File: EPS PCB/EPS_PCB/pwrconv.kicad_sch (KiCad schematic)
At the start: 27 parts, among them U1 TPS5430DDA, U2 TPS5430DDA, U3 TPS5430DDA

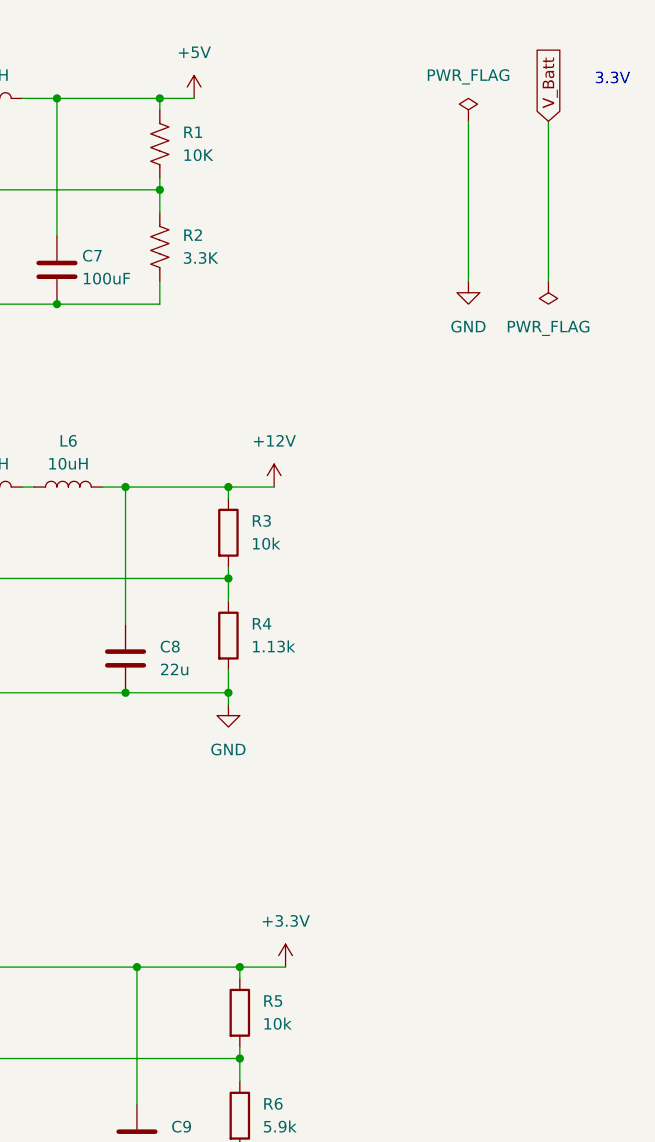
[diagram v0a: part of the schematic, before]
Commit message: PDR Update
Added Current Measurement, Hysteresis, EFuses
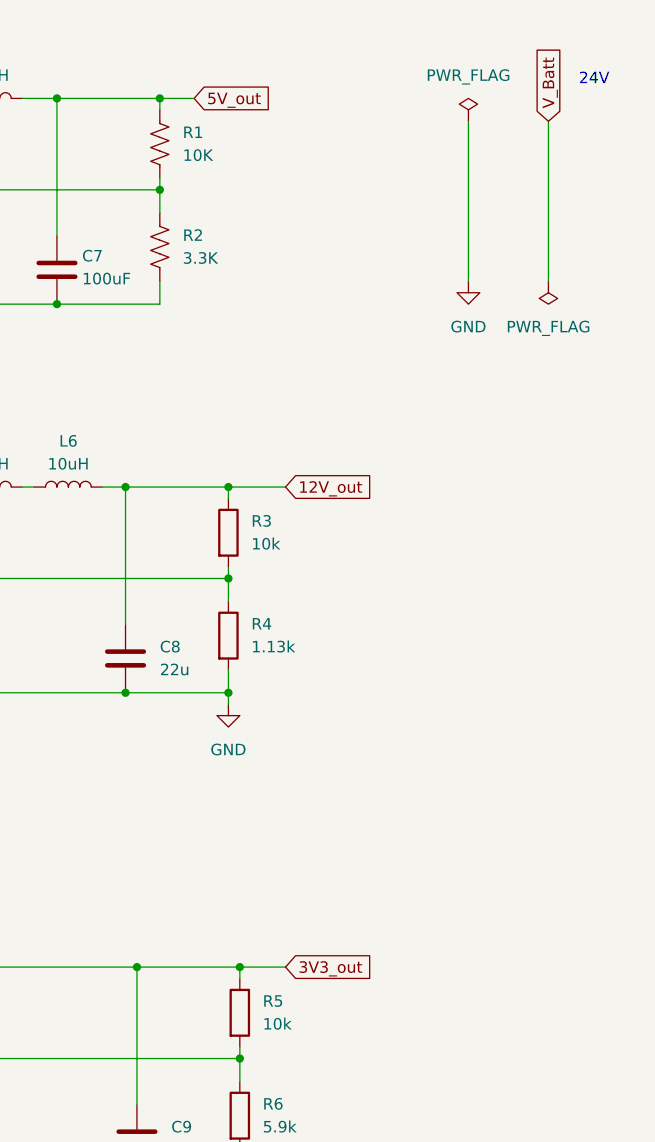
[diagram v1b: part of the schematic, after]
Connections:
- net +12V renamed 12V_out
- net +3.3V renamed 3V3_out
- net +5V renamed 5V_out
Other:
- note added: "24V"
- note removed: "3.3V"
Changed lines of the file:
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@@
 		(date "2024-11-14")
 		(company "UW Huskysat")
-		(comment 1 "Tracy, Maria, Phina, David")
-	)
-	(text "3.3V\n"
+		(comment 1 "Tracy, Maria, Phina, David, Chase")
+	)
+	(text "24V\n"
 		(exclude_from_sim no)
-		(at 188.722 22.098 0)
+		(at 186.69 22.098 0)
 		(effects
 			(font
@@
 	(wire
 		(pts
-			(xy 146.05 67.31) (xy 151.13 67.31)
+			(xy 146.05 67.31) (xy 152.4 67.31)
 		)
 		(stroke
@@
 		)
 	)
+	(global_label "3V3_out"
+		(shape input)
+		(at 152.4 120.65 0)
+		(fields_autoplaced yes)
+		(effects
+			(font
+				(size 1.27 1.27)
+			)
+			(justify left)
+		)
+		(property "Intersheetrefs" "${INTERSHEET_REFS}"
+			(at 162.8841 120.65 0)
+			(effects
+				(font
+					(size 1.27 1.27)
+				)
+				(justify left)
+				(hide yes)
+			)
+		)
+	)
 	(global_label "V_Batt"
 		(shape input)
@@
 				)
 				(justify right)
+				(hide yes)
+			)
+		)
+	)
+	(global_label "5V_out"
+		(shape input)
+		(at 142.24 24.13 0)
+		(fields_autoplaced yes)
+		(effects
+			(font
+				(size 1.27 1.27)
+			)
+			(justify left)
+		)
+		(property "Intersheetrefs" "${INTERSHEET_REFS}"
+			(at 151.5146 24.13 0)
+			(effects
+				(font
+					(size 1.27 1.27)
+				)
+				(justify left)
+				(hide yes)
+			)
+		)
+	)
+	(global_label "12V_out"
+		(shape input)
+		(at 152.4 67.31 0)
+		(fields_autoplaced yes)
+		(effects
+			(font
+				(size 1.27 1.27)
+			)
+			(justify left)
+		)
+		(property "Intersheetrefs" "${INTERSHEET_REFS}"
+			(at 162.8841 67.31 0)
+			(effects
+				(font
+					(size 1.27 1.27)
+				)
+				(justify left)
 				(hide yes)
 			)
@@
 	)
 	(symbol
-		(lib_id "power:+12V")
-		(at 151.13 67.31 0)
-		(unit 1)
-		(exclude_from_sim no)
-		(in_bom yes)
-		(on_board yes)
-		(dnp no)
-		(fields_autoplaced yes)
-		(property "Reference" "#PWR014"
-			(at 151.13 71.12 0)
-			(effects
-				(font
-					(size 1.27 1.27)
-				)
-				(hide yes)
-			)
-		)
-		(property "Value" "+12V"
-			(at 151.13 62.23 0)
-			(effects
-				(font
-					(size 1.27 1.27)
-				)
-			)
-		)
-		(property "Footprint" ""
-			(at 151.13 67.31 0)
-			(effects
-				(font
-					(size 1.27 1.27)
-				)
-				(hide yes)
-			)
-		)
-		(property "Datasheet" ""
-			(at 151.13 67.31 0)
-			(effects
-				(font
-					(size 1.27 1.27)
-				)
-				(hide yes)
-			)
-		)
-		(property "Description" "Power symbol creates a global label with name \"+12V\""
-			(at 151.13 67.31 0)
-			(effects
-				(font
-					(size 1.27 1.27)
-				)
-				(hide yes)
-			)
-		)
-		(pin "1"
-		)
-		(instances
-			(project ""
-				(path "/7c207afd-2547-4b3f-ab21-327d2c978d3b"
-					(reference "#PWR?")
-					(unit 1)
-				)
-			)
-			(project ""
-				(path "/e5aefcdf-1552-4881-b70a-fd78aade4bcb/b0e0f9e9-e39c-4f93-a8b5-ddf6770a9a8d"
-					(reference "#PWR014")
-					(unit 1)
-				)
-			)
-		)
-	)
-	(symbol
 		(lib_id "Regulator_Switching:TPS5430DDA")
 		(at 73.66 125.73 0)
@@
 					(unit 1)
 				)
-			)
-		)
-	)
-	(symbol
-		(lib_id "power:+12V")
-		(at 152.4 120.65 0)
-		(unit 1)
-		(exclude_from_sim no)
-		(in_bom yes)
-		(on_board yes)
-		(dnp no)
-		(fields_autoplaced yes)
-		(property "Reference" "#PWR015"
-			(at 152.4 124.46 0)
-			(effects
-				(font
-					(size 1.27 1.27)
-				)
-				(hide yes)
-			)
-		)
-		(property "Value" "+3.3V"
-			(at 152.4 115.57 0)
-			(effects
-				(font
-					(size 1.27 1.27)
-				)
-			)
-		)
-		(property "Footprint" ""
-			(at 152.4 120.65 0)
-			(effects
-				(font
-					(size 1.27 1.27)
-				)
-				(hide yes)
-			)
-		)
-		(property "Datasheet" ""
-			(at 152.4 120.65 0)
-			(effects
-				(font
-					(size 1.27 1.27)
-				)
-				(hide yes)
-			)
-		)
-		(property "Description" "Power symbol creates a global label with name \"+12V\""
-			(at 152.4 120.65 0)
-			(effects
-				(font
-					(size 1.27 1.27)
-				)
-				(hide yes)
-			)
-		)
-		(pin "1"
-		)
-		(instances
-			(project "pwrconv"
-				(path "/7c207afd-2547-4b3f-ab21-327d2c978d3b"
-					(reference "#PWR?")
-					(unit 1)
-				)
-			)
-			(project "pwrconv"
-				(path "/e5aefcdf-1552-4881-b70a-fd78aade4bcb/b0e0f9e9-e39c-4f93-a8b5-ddf6770a9a8d"
-					(reference "#PWR015")
-					(unit 1)
-				)
-			)
-		)
-	)
-	(symbol
-		(lib_id "power:+5V")
-		(at 142.24 24.13 0)
-		(unit 1)
-		(exclude_from_sim no)
-		(in_bom yes)
-		(on_board yes)
-		(dnp no)
-		(fields_autoplaced yes)
-		(property "Reference" "#PWR011"
-			(at 142.24 27.94 0)
-			(effects
-				(font
-					(size 1.27 1.27)
-				)
-				(hide yes)
-			)
-		)
-		(property "Value" "+5V"
-			(at 142.24 19.05 0)
-			(effects
-				(font
-					(size 1.27 1.27)
-				)
-			)
-		)
-		(property "Footprint" ""
-			(at 142.24 24.13 0)
-			(effects
-				(font
-					(size 1.27 1.27)
-				)
-				(hide yes)
-			)
-		)
-		(property "Datasheet" ""
-			(at 142.24 24.13 0)
-			(effects
-				(font
-					(size 1.27 1.27)
-				)
-				(hide yes)
-			)
-		)
-		(property "Description" "Power symbol creates a global label with name \"+5V\""
-			(at 142.24 24.13 0)
-			(effects
-				(font
-					(size 1.27 1.27)
-				)
-				(hide yes)
-			)
-		)
-		(pin "1"
-		)
-		(instances
-			(project "pwrconv"
-				(path "/7c207afd-2547-4b3f-ab21-327d2c978d3b"
-					(reference "#PWR?")
-					(unit 1)
-				)
-			)
-			(project "pwrconv"
-				(path "/e5aefcdf-1552-4881-b70a-fd78aade4bcb/b0e0f9e9-e39c-4f93-a8b5-ddf6770a9a8d"
-					(reference "#PWR011")
-					(unit 1)
-				)
